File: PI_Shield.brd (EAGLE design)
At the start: 69 x 65.2 mm, 64 parts, among them J10 T2I, J11 T2I, J12 T2I, J13 DF13-4P-1.25DSA, J14 DF13-4P-1.25DSA, J15 DF13-4P-1.25DSA, J16 T2I5P, Q1 220mA/50V/3.5Ω, Q3 220mA/50V/3.5Ω, Q4 220mA/50V/3.5Ω, Q5 2.5A/30V/105mΩ, U1 MAX1136EUA-T, U2 AZ1117EH-3.3TRG1, Y1 ECS-80-S-4X

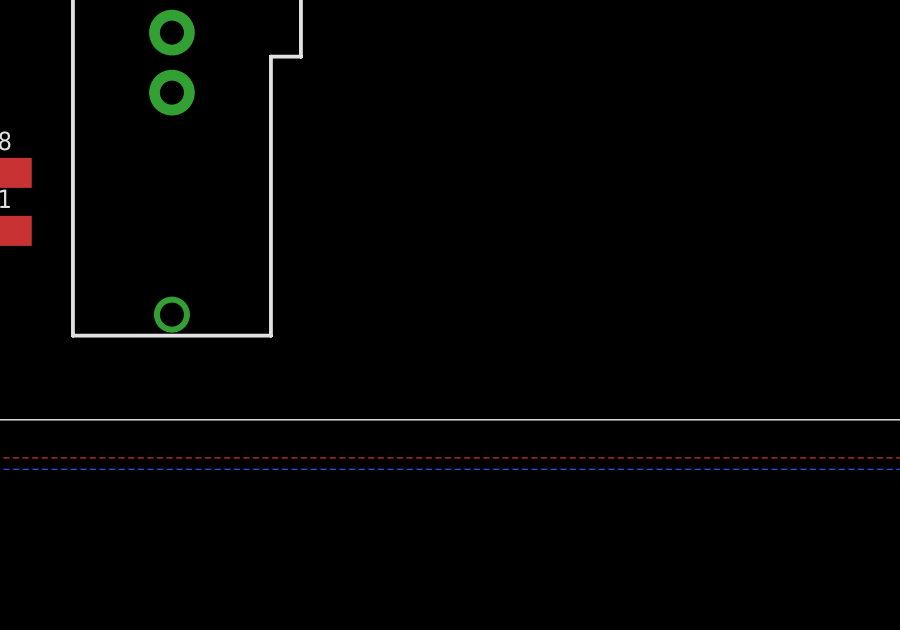
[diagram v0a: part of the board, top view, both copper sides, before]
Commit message: add micro usb connector for external powering while testing
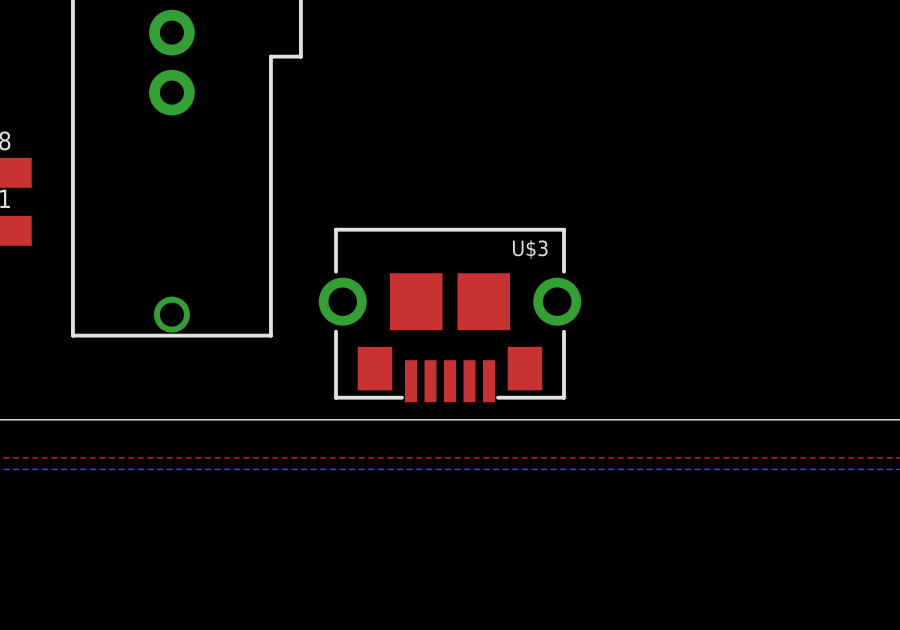
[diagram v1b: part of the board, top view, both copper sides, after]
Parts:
- added U$3: USB-MICRO, usb conn:MICRO-USB
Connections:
- net 5V: now also U$3.1
- net GND: now also U$3.5, U$3.SHLD@1, U$3.SHLD@2, U$3.SHLD@3, U$3.SHLD@4, U$3.SHLD@5, U$3.SHLD@6
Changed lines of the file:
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@@
 <attribute name="VALUE" x="-1.397" y="-105.537" size="0.6096" layer="27" font="vector" ratio="20"/>
+</element>
+<element name="U$3" library="usb conn" package="MICRO-USB" value="USB-MICRO" x="33.147" y="3.937" smashed="yes" rot="R180">
+<attribute name="NAME" x="36.449" y="5.969" size="0.508" layer="21" rot="R180"/>
 </element>
 </elements>
@@
 <contactref element="U$5" pad="GND"/>
 <contactref element="U$4" pad="GND"/>
+<contactref element="U$3" pad="SHLD@1"/>
+<contactref element="U$3" pad="SHLD@2"/>
+<contactref element="U$3" pad="SHLD@6"/>
+<contactref element="U$3" pad="SHLD@5"/>
+<contactref element="U$3" pad="SHLD@3"/>
+<contactref element="U$3" pad="SHLD@4"/>
+<contactref element="U$3" pad="5"/>
+<wire x1="34.272" y1="3.937" x2="36.722" y2="3.937" width="0" layer="19" extent="1-1"/>
+<wire x1="32.022" y1="3.937" x2="34.272" y2="3.937" width="0" layer="19" extent="1-1"/>
+<wire x1="29.572" y1="3.937" x2="32.022" y2="3.937" width="0" layer="19" extent="1-1"/>
+<wire x1="35.647" y1="1.707" x2="36.722" y2="3.937" width="0" layer="19" extent="1-1"/>
+<wire x1="30.647" y1="1.707" x2="29.572" y2="3.937" width="0" layer="19" extent="1-1"/>
+<wire x1="31.847" y1="1.287" x2="30.647" y2="1.707" width="0" layer="19" extent="1-1"/>
+<wire x1="-3.75" y1="-145.542" x2="29.572" y2="3.937" width="0" layer="19" extent="1-1"/>
 <wire x1="-3.75" y1="-132.842" x2="-3.75" y2="-145.542" width="0" layer="19" extent="1-1"/>
 <wire x1="-3.75" y1="-120.142" x2="-3.75" y2="-132.842" width="0" layer="19" extent="1-1"/>
@@
 <contactref element="J16" pad="2"/>
 <contactref element="R16" pad="2"/>
-<wire x1="114.6556" y1="2.9464" x2="119.0244" y2="4.9276" width="0" layer="19" extent="1-1"/>
+<contactref element="U$3" pad="1"/>
+<wire x1="4.1656" y1="-31.877" x2="34.447" y2="1.287" width="0" layer="19" extent="1-1"/>
+<wire x1="18.6554" y1="6.2992" x2="4.1656" y2="-31.877" width="0" layer="19" extent="1-1"/>
+<wire x1="18.6554" y1="8.2296" x2="18.6554" y2="6.2992" width="0" layer="19" extent="1-1"/>
+<wire x1="23.878" y1="10.906" x2="18.6554" y2="8.2296" width="0" layer="19" extent="1-1"/>
+<wire x1="23.878" y1="12.906" x2="23.878" y2="10.906" width="0" layer="19" extent="1-1"/>
+<wire x1="77.724" y1="31.242" x2="23.878" y2="12.906" width="0" layer="19" extent="1-1"/>
+<wire x1="114.6556" y1="2.9464" x2="77.724" y2="31.242" width="0" layer="19" extent="1-1"/>
+<wire x1="119.0244" y1="4.9276" x2="114.6556" y2="2.9464" width="0" layer="19" extent="1-1"/>
 <wire x1="121.92" y1="-28.36" x2="114.6556" y2="2.9464" width="0" layer="19" extent="1-1"/>
 <wire x1="127" y1="-28.11" x2="121.92" y2="-28.36" width="0" layer="19" extent="1-1"/>
@@
 <wire x1="105.41" y1="-44.87" x2="107.1" y2="-38.1" width="0" layer="19" extent="1-1"/>
 <wire x1="99.3394" y1="-44.87" x2="105.41" y2="-44.87" width="0" layer="19" extent="1-1"/>
-<wire x1="77.724" y1="31.242" x2="114.6556" y2="2.9464" width="0" layer="19" extent="1-1"/>
-<wire x1="23.878" y1="12.906" x2="77.724" y2="31.242" width="0" layer="19" extent="1-1"/>
-<wire x1="23.878" y1="10.906" x2="23.878" y2="12.906" width="0" layer="19" extent="1-1"/>
-<wire x1="18.6554" y1="8.2296" x2="23.878" y2="10.906" width="0" layer="19" extent="1-1"/>
-<wire x1="18.6554" y1="6.2992" x2="18.6554" y2="8.2296" width="0" layer="19" extent="1-1"/>
-<wire x1="4.1656" y1="-31.877" x2="18.6554" y2="6.2992" width="0" layer="19" extent="1-1"/>
 <wire x1="-1.2726" y1="74.9614" x2="23.878" y2="12.906" width="0" layer="19" extent="1-1"/>
 </signal>

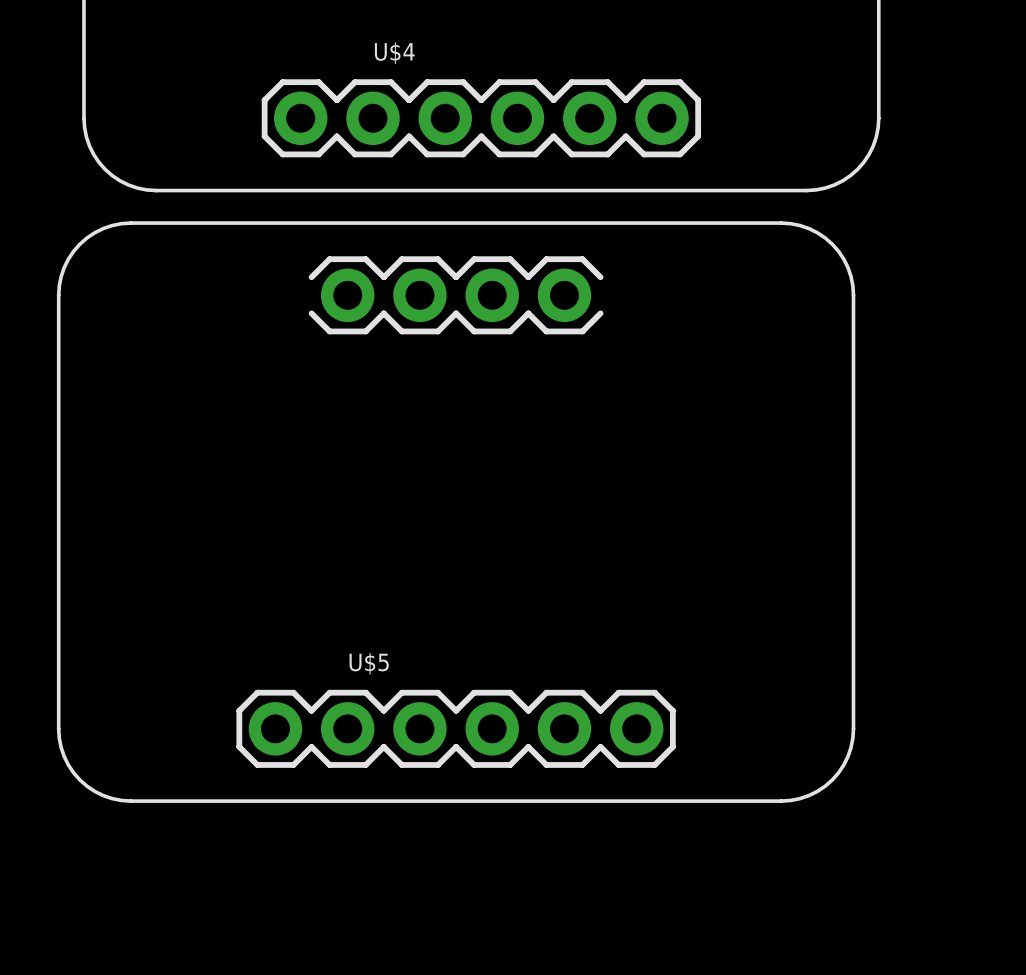
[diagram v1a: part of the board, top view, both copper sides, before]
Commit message: update bno055 footprint
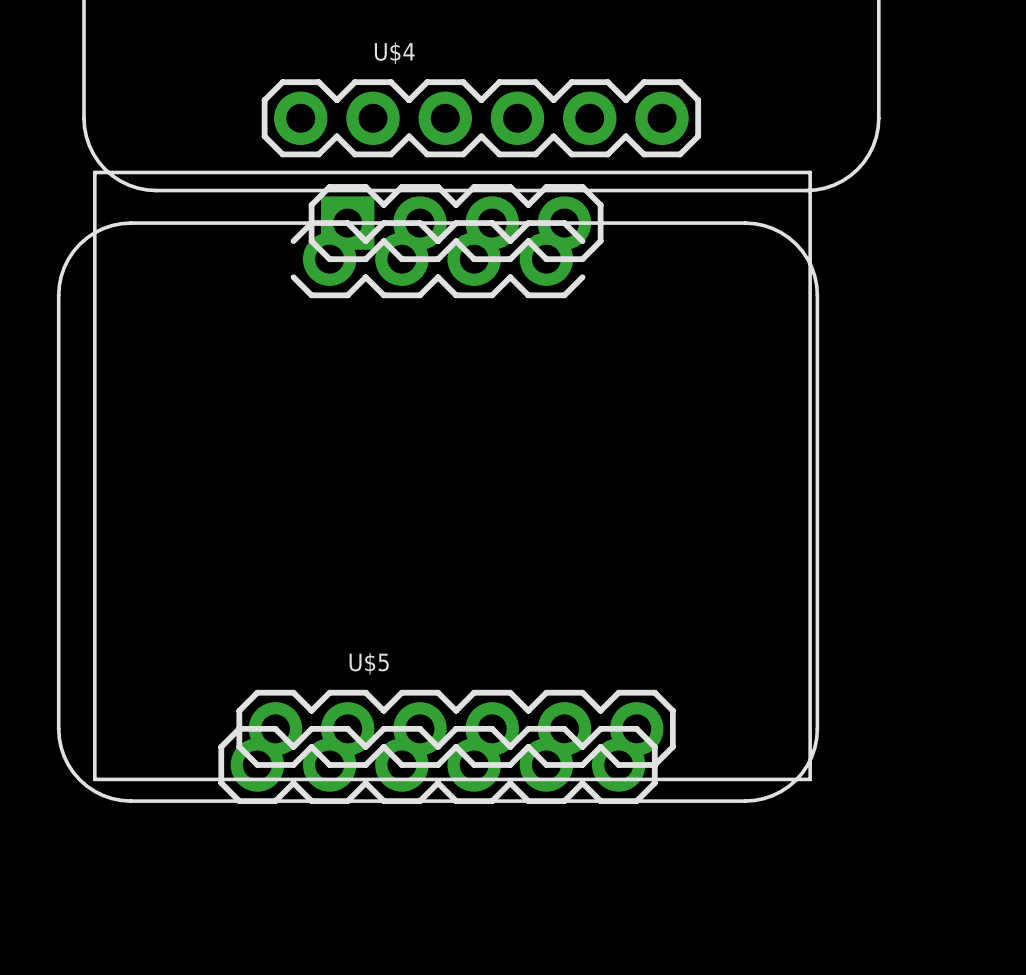
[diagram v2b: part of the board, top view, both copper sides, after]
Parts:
- added U$6: BNO055_9DOF_BREAKOUT, Other:BNO055
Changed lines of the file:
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@@
 <attribute name="NAME" x="36.449" y="5.969" size="0.508" layer="21" rot="R180"/>
 </element>
+<element name="U$6" library="Other" package="BNO055" value="BNO055_9DOF_BREAKOUT" x="-5.207" y="-98.552" smashed="yes" rot="R90"/>
 </elements>
 <signals>
@@
 <contactref element="U$3" pad="SHLD@4"/>
 <contactref element="U$3" pad="5"/>
-<wire x1="34.272" y1="3.937" x2="36.722" y2="3.937" width="0" layer="19" extent="1-1"/>
-<wire x1="32.022" y1="3.937" x2="34.272" y2="3.937" width="0" layer="19" extent="1-1"/>
-<wire x1="29.572" y1="3.937" x2="32.022" y2="3.937" width="0" layer="19" extent="1-1"/>
-<wire x1="35.647" y1="1.707" x2="36.722" y2="3.937" width="0" layer="19" extent="1-1"/>
-<wire x1="30.647" y1="1.707" x2="29.572" y2="3.937" width="0" layer="19" extent="1-1"/>
-<wire x1="31.847" y1="1.287" x2="30.647" y2="1.707" width="0" layer="19" extent="1-1"/>
-<wire x1="-3.75" y1="-145.542" x2="29.572" y2="3.937" width="0" layer="19" extent="1-1"/>
 <wire x1="-3.75" y1="-132.842" x2="-3.75" y2="-145.542" width="0" layer="19" extent="1-1"/>
 <wire x1="-3.75" y1="-120.142" x2="-3.75" y2="-132.842" width="0" layer="19" extent="1-1"/>
-<wire x1="-5.207" y1="-107.442" x2="-3.75" y2="-120.142" width="0" layer="19" extent="1-1"/>
-<wire x1="-4.318" y1="-85.979" x2="-5.207" y2="-107.442" width="0" layer="19" extent="1-1"/>
+<wire x1="-5.842" y1="-108.712" x2="-3.75" y2="-120.142" width="0" layer="19" extent="1-1"/>
+<wire x1="-4.318" y1="-85.979" x2="-5.842" y2="-108.712" width="0" layer="19" extent="1-1"/>
 <wire x1="-14.517" y1="-63.754" x2="-4.318" y2="-85.979" width="0" layer="19" extent="1-1"/>
 <wire x1="-14.517" y1="-60.452" x2="-14.517" y2="-63.754" width="0" layer="19" extent="1-1"/>
@@
 <wire x1="23.878" y1="18.906" x2="13.5382" y2="18.5166" width="0" layer="19" extent="1-1"/>
 <wire x1="23.878" y1="16.906" x2="23.878" y2="18.906" width="0" layer="19" extent="1-1"/>
+<wire x1="29.572" y1="3.937" x2="23.878" y2="16.906" width="0" layer="19" extent="1-1"/>
+<wire x1="32.022" y1="3.937" x2="29.572" y2="3.937" width="0" layer="19" extent="1-1"/>
+<wire x1="34.272" y1="3.937" x2="32.022" y2="3.937" width="0" layer="19" extent="1-1"/>
+<wire x1="36.722" y1="3.937" x2="34.272" y2="3.937" width="0" layer="19" extent="1-1"/>
+<wire x1="35.647" y1="1.707" x2="36.722" y2="3.937" width="0" layer="19" extent="1-1"/>
+<wire x1="30.647" y1="1.707" x2="29.572" y2="3.937" width="0" layer="19" extent="1-1"/>
+<wire x1="31.847" y1="1.287" x2="30.647" y2="1.707" width="0" layer="19" extent="1-1"/>
 <wire x1="4.7274" y1="74.9614" x2="13.5382" y2="56.6166" width="0" layer="19" extent="1-1"/>
 <wire x1="-12.827" y1="41.656" x2="10.9982" y2="43.9166" width="0" layer="19" extent="1-1"/>
-<wire x1="73.787" y1="10.414" x2="23.878" y2="16.906" width="0" layer="19" extent="1-1"/>
+<wire x1="73.787" y1="10.414" x2="36.722" y2="3.937" width="0" layer="19" extent="1-1"/>
 <wire x1="77.724" y1="15.367" x2="73.787" y2="10.414" width="0" layer="19" extent="1-1"/>
 <wire x1="77.724" y1="23.622" x2="77.724" y2="15.367" width="0" layer="19" extent="1-1"/>
@@
 <wire x1="0" y1="-132.842" x2="0" y2="-145.542" width="0" layer="19" extent="1-1"/>
 <wire x1="0" y1="-120.142" x2="0" y2="-132.842" width="0" layer="19" extent="1-1"/>
-<wire x1="-10.287" y1="-107.442" x2="0" y2="-120.142" width="0" layer="19" extent="1-1"/>
-<wire x1="-9.398" y1="-85.979" x2="-10.287" y2="-107.442" width="0" layer="19" extent="1-1"/>
+<wire x1="-10.922" y1="-108.712" x2="0" y2="-120.142" width="0" layer="19" extent="1-1"/>
+<wire x1="-9.398" y1="-85.979" x2="-10.922" y2="-108.712" width="0" layer="19" extent="1-1"/>
 <wire x1="-16.217" y1="-67.056" x2="-9.398" y2="-85.979" width="0" layer="19" extent="1-1"/>
 <wire x1="0.6486" y1="-27.9908" x2="-16.217" y2="-67.056" width="0" layer="19" extent="1-1"/>
@@
 <wire x1="-2.5" y1="-132.842" x2="-2.5" y2="-145.542" width="0" layer="19" extent="1-1"/>
 <wire x1="-2.5" y1="-120.142" x2="-2.5" y2="-132.842" width="0" layer="19" extent="1-1"/>
-<wire x1="-2.667" y1="-107.442" x2="-2.5" y2="-120.142" width="0" layer="19" extent="1-1"/>
-<wire x1="0.762" y1="-85.979" x2="-2.667" y2="-107.442" width="0" layer="19" extent="1-1"/>
+<wire x1="-3.302" y1="-108.712" x2="-2.5" y2="-120.142" width="0" layer="19" extent="1-1"/>
+<wire x1="0.762" y1="-85.979" x2="-3.302" y2="-108.712" width="0" layer="19" extent="1-1"/>
 <wire x1="13.5382" y1="10.8966" x2="0.762" y2="-85.979" width="0" layer="19" extent="1-1"/>
 <wire x1="73.787" y1="5.334" x2="13.5382" y2="10.8966" width="0" layer="19" extent="1-1"/>
@@
 <wire x1="-1.25" y1="-132.842" x2="-1.25" y2="-145.542" width="0" layer="19" extent="1-1"/>
 <wire x1="-1.25" y1="-120.142" x2="-1.25" y2="-132.842" width="0" layer="19" extent="1-1"/>
-<wire x1="-0.127" y1="-107.442" x2="-1.25" y2="-120.142" width="0" layer="19" extent="1-1"/>
-<wire x1="-1.778" y1="-85.979" x2="-0.127" y2="-107.442" width="0" layer="19" extent="1-1"/>
+<wire x1="-0.762" y1="-108.712" x2="-1.25" y2="-120.142" width="0" layer="19" extent="1-1"/>
+<wire x1="-1.778" y1="-85.979" x2="-0.762" y2="-108.712" width="0" layer="19" extent="1-1"/>
 <wire x1="13.5382" y1="13.4366" x2="-1.778" y2="-85.979" width="0" layer="19" extent="1-1"/>
 <wire x1="73.787" y1="7.874" x2="13.5382" y2="13.4366" width="0" layer="19" extent="1-1"/>
@@
 <contactref element="PCB1" pad="11"/>
 <contactref element="U$5" pad="RST"/>
-<wire x1="13.5382" y1="21.0566" x2="2.413" y2="-107.442" width="0" layer="19" extent="1-1"/>
+<wire x1="13.5382" y1="21.0566" x2="1.778" y2="-108.712" width="0" layer="19" extent="1-1"/>
 </signal>
 <signal name="5V" class="2">
@@
 <contactref element="PCB1" pad="13"/>
 <contactref element="U$5" pad="INT"/>
-<wire x1="13.5382" y1="23.5966" x2="-2.667" y2="-92.202" width="0" layer="19" extent="1-1"/>
+<wire x1="13.5382" y1="23.5966" x2="-3.302" y2="-90.932" width="0" layer="19" extent="1-1"/>
 </signal>
 <signal name="DI">
@@
 <contactref element="U$4" pad="3VO"/>
 <contactref element="U$5" pad="3VO"/>
-<wire x1="-6.858" y1="-85.979" x2="-7.747" y2="-107.442" width="0" layer="19" extent="1-1"/>
+<wire x1="-6.858" y1="-85.979" x2="-8.382" y2="-108.712" width="0" layer="19" extent="1-1"/>
 </signal>
 <signal name="N$1">
 <contactref element="R20" pad="2"/>
 <contactref element="U$5" pad="ADR"/>
-<wire x1="-14.517" y1="-67.056" x2="-0.127" y2="-92.202" width="0" layer="19" extent="1-1"/>
+<wire x1="-14.517" y1="-67.056" x2="-0.762" y2="-90.932" width="0" layer="19" extent="1-1"/>
 </signal>
 </signals>

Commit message: Added Pi 4 and Current Sensor; Routed Interrupt pins signals to Pi
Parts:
- removed PCB1: RPI2, RaspberryPi:RPI2
- added C10, C14: 0.1uF, SparkFun-Capacitors:0603
- added Q2: 220mA/50V/3.5Ω, SparkFun-DiscreteSemi:SOT23-3
- added R22: 0, SparkFun-Resistors:0603
- added R23, R25: 10k, SparkFun-Resistors:0603
- added R24: 1k, SparkFun-Resistors:0603
- added U$7: MCR1101, MCR1101:MCR1101
- added U$8: RPI4, RaspberryPi:RPI4
- U$6: value BNO055_9DOF_BREAKOUT -> (none); device Other:BNO055 -> Push button - FSM2JMTR:DISCRETECOMPONENTS_SW_2512
- moved U$6 98.5 mm to (-59.1, -181.0), turned to 0 degrees
- moved Q4 1.77 mm to (112.9, -48.1), turned to 0 degrees
- moved Q1 0.74 mm to (99.7, -33.4), turned to 0 degrees
- moved Q3 0.52 mm to (104.9, -50.9), turned to 0 degrees
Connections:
- removed net AMP_FAULT: Q5.1, R16.1
- removed net N$4: U$1.11
- removed net N$5: U$1.10
- removed net RESET_TO_PI: PCB1.15, R10.2
- new net !AMP_FAULT: Q5.1, R16.1, U$7.!FAULTB
- new net !AMP_RESET: Q2.1, R25.2, U$6.1, U$8.7
- new net 5V_RAW: J16.1, J16.2, R22.2, U$3.1, U$7.IP+, U$7.IP+@2, U$7.IP+@3, U$7.IP+@4
- new net 9DOF_RST: U$4.RST, U$8.32
- new net A_INT: U$4.AI1, U$8.26
- new net CAN_RESET: R10.2, U$8.15
- new net G_INT: U$4.GI1, U$8.22
- new net N$13: Q2.3, R24.1
- new net N$6: C14.1, U$7.VCAP
- new net OCD: R23.1, R24.2, U$7.VOC
- new net RX0_INT: U$1.11, U$8.37
- new net RX1_INT: U$1.10, U$8.29
- net 3V3: now also R25.1
- net 5V: now also C10.1, Q5.2, R22.1, R23.2, U$7.IP-, U$7.IP-@2, U$7.IP-@3, U$7.IP-@4, U$7.VCC; no longer J16.1, J16.2, Q5.3, U$3.1
- net AMP_OUT: now also U$7.VOUT
- net CLK: now also U$8.23; no longer PCB1.23
- net CS: now also U$8.24; no longer PCB1.24
- net DI: now also U$8.31; no longer PCB1.31
- net DI1: now also U$8.36; no longer PCB1.36
- net DI2: now also U$8.38; no longer PCB1.38
- net DI3: now also U$8.40; no longer PCB1.40
- net GND: now also C10.2, C14.2, Q2.2, U$6.2, U$7.GND, U$7.GND@2, U$7.GND@3, U$8.14, U$8.20, U$8.25, U$8.30, U$8.34, U$8.39, U$8.6, U$8.9; no longer PCB1.14, PCB1.20, PCB1.25, PCB1.30, PCB1.34, PCB1.39, PCB1.6, PCB1.9
- net IMU_INT: now also U$8.13; no longer PCB1.13
- net IMU_RESET: now also U$8.11; no longer PCB1.11
- net INT: now also U$8.35; no longer PCB1.35
- net MISO: now also U$8.21; no longer PCB1.21
- net MOSI: now also U$8.19; no longer PCB1.19
- net N$10: now also Q5.3; no longer Q5.2
- net PI_POWER: now also U$8.2, U$8.4; no longer PCB1.2, PCB1.4
- net PWM: now also U$8.33; no longer PCB1.33
- net RX: now also U$8.10; no longer PCB1.10
- net SCL: now also U$8.5; no longer PCB1.5
- net SDA: now also U$8.3; no longer PCB1.3
- net TX: now also U$8.8; no longer PCB1.8

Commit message: Started layout
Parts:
- moved R25 292.7 mm to (-91.4, 115.6)
- moved R24 281.5 mm to (-87.6, 115.6)
- moved R23 277.9 mm to (-83.8, 115.6)
- moved U$8 274.9 mm to (64.8, 3.81), turned to 90 degrees
- moved R2 273.8 mm to (-106.7, 110.5), turned to 0 degrees
- moved C14 271.2 mm to (-99.1, 110.5)
- moved D4 271.2 mm to (-99.1, 114.3)
- moved Q2 268.6 mm to (-41.9, 97.8)
- moved C13 268.2 mm to (-95.2, 110.5), turned to 0 degrees
- moved R22 267.7 mm to (-80.0, 115.6)
- moved C10 266.2 mm to (-83.8, 110.5)
- moved R1 264.7 mm to (-102.9, 110.5), turned to 0 degrees
- moved C6 252.7 mm to (-72.4, 110.5), flipped to the top, turned to 0 degrees
- moved R17 244.4 mm to (-64.8, 115.6), turned to 0 degrees
- moved C12 243.3 mm to (-91.4, 110.5), turned to 0 degrees
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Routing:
- removed copper zone on layer 1, net GND
- removed copper zone on layer 16, net GND
- removed copper zone on layer 1, net PI_POWER
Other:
- board size 69 x 65.2 mm -> 72.4 x 72.4 mm
- board text removed: "ROV X13 PI Shield v1 DATE NAME"

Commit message: Continuing Layout
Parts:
- C14: value 0.1uF -> .01uF
- moved C14 154.6 mm to (25.9, 19.4), flipped to the bottom, turned to 270 degrees
- moved R3 153.9 mm to (37.3, 67.8)
- moved R2 152.8 mm to (30.6, 43.4), turned to 270 degrees
- moved R24 150.8 mm to (25.9, 16.4), flipped to the bottom, turned to 270 degrees
- moved R22 148.5 mm to (33.7, 20.1), turned to 270 degrees
- moved R25 148.1 mm to (28.2, 28.2), flipped to the bottom, turned to 180 degrees
- moved C10 146.4 mm to (30.4, 18.9), flipped to the bottom, turned to 90 degrees
- moved R1 145.7 mm to (27.4, 45.2), flipped to the bottom, turned to 270 degrees
- moved C11 141.9 mm to (32.8, 35.3), turned to 90 degrees
- moved R23 140.6 mm to (19.7, 20.4), flipped to the bottom, turned to 90 degrees
- moved C8 134.4 mm to (26.8, 24.1), flipped to the bottom, turned to 270 degrees
- moved C12 133.1 mm to (22.2, 41.3), turned to 270 degrees
- moved R12 129.5 mm to (51.8, 30.4)
- moved R15 129.5 mm to (40.4, 30.4)
- moved C9 128.3 mm to (18.2, 27.8), flipped to the bottom, turned to 90 degrees
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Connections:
- net CAN_H renamed CAN_P
- net CAN_L renamed CAN_N

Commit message: Finished Layout
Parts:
- moved R20 169.5 mm to (45.5, 19.8), flipped to the bottom, turned to 180 degrees
- moved D4 160.2 mm to (29.2, 18.3), turned to 270 degrees
- moved C13 152.0 mm to (37.6, 36.7), flipped to the bottom, turned to 90 degrees
- moved R21 146.9 mm to (17.7, 2.54), turned to 270 degrees
- moved R18 140.6 mm to (15.1, 2.54), turned to 270 degrees
- moved R17 133.8 mm to (27.1, 18.3), turned to 270 degrees
- moved R16 131.6 mm to (22.9, 14.1), flipped to the bottom, turned to 90 degrees
- moved R9 121.3 mm to (43.7, 22.6), flipped to the bottom
- moved Q5 118.0 mm to (26.0, 14.1), flipped to the bottom, turned to 90 degrees
- moved R8 117.0 mm to (43.7, 25.1), flipped to the bottom
- moved J6 36.2 mm to (37.0, 42.5), turned to 180 degrees
- moved J1 32.2 mm to (67.4, 42.9), turned to 270 degrees
- moved Q3 31.7 mm to (39.1, 12.1), flipped to the bottom, turned to 270 degrees
- moved J9 30.4 mm to (29.5, 24.6), turned to 180 degrees
- moved J7 27.6 mm to (62.2, 37.7), turned to 270 degrees
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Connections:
- removed net 9DOF_RST: U$4.RST, U$8.32
- net IMU_RESET: now also U$4.RST
